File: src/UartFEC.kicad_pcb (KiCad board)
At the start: 2 copper layers, 24 x 27.9 mm, 16 parts, among them J1 B3B-XH-A, P1 105444-0001, U1 FT232RL

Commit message: Minor resistor move
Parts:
- moved R1 0.10 mm to (23.6, 44.1)
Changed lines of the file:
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@@
         (effects (font (size 0.8 0.6) (thickness 0.15)))
     )
-    (fp_text value "1K" (at 0 1.7) (layer "F.SilkS")
+    (fp_text value "1K" (at 0 1.5) (layer "F.SilkS")
         (effects (font (size 0.8 0.6) (thickness 0.15)))
     )
@@
   )
   (footprint "Medo64:R (0805)" (layer "F.Cu")
-    (at 23.7 44.1 180)
+    (at 23.6 44.1 180)
     (tags "RESC2013X70N")
     (attr smd)
@@
         (effects (font (size 0.8 0.6) (thickness 0.15)))
     )
-    (fp_text value "1K" (at 0 1.7) (layer "F.SilkS")
+    (fp_text value "1K" (at 0 1.5) (layer "F.SilkS")
         (effects (font (size 0.8 0.6) (thickness 0.15)))
     )
@@
   (segment (start 34.475 33.625) (end 35.5 33.625) (width 0.35) (layer "F.Cu") (net 2))
   (segment (start 32.95 35.15) (end 34.475 33.625) (width 0.35) (layer "F.Cu") (net 2))
-  (segment (start 23.556148 39.656148) (end 23.556148 42.756148) (width 0.2) (layer "F.Cu") (net 3))
   (segment (start 43.211786 36.988214) (end 43.208226 36.9881) (width 0.2) (layer "F.Cu") (net 3))
   (segment (start 43.3 27.6) (end 43.6 27.9) (width 0.2) (layer "F.Cu") (net 3))
@@
   (segment (start 42.5 26.6) (end 42.5 27.6) (width 0.2) (layer "F.Cu") (net 3))
   (segment (start 28.5 28.525) (end 26.8 28.525) (width 0.2) (layer "F.Cu") (net 3))
-  (segment (start 21.7 36.5) (end 23.510568 38.310568) (width 0.2) (layer "F.Cu") (net 3))
   (segment (start 40.400008 27.6) (end 42.5 27.6) (width 0.2) (layer "F.Cu") (net 3))
   (segment (start 43.6 36.6) (end 43.211786 36.988214) (width 0.2) (layer "F.Cu") (net 3))
+  (segment (start 23.556148 43.106148) (end 24.55 44.1) (width 0.2) (layer "F.Cu") (net 3))
+  (segment (start 23.556148 39.656148) (end 23.556148 43.106148) (width 0.2) (layer "F.Cu") (net 3))
   (segment (start 26.725 28.6) (end 26.8 28.525) (width 0.2) (layer "F.Cu") (net 3))
   (segment (start 43.208226 36.9881) (end 43.08487 37) (width 0.2) (layer "F.Cu") (net 3))
   (segment (start 40.4 27.599992) (end 40.400008 27.6) (width 0.2) (layer "F.Cu") (net 3))
   (segment (start 40.4 26.55) (end 40.4 27.599992) (width 0.2) (layer "F.Cu") (net 3))
+  (segment (start 21.7 36.5) (end 23.510568 38.310568) (width 0.2) (layer "F.Cu") (net 3))
   (segment (start 21.7 36.5) (end 21.3 36.1) (width 0.2) (layer "F.Cu") (net 3))
   (segment (start 40.436628 43.086628) (end 41.4 44.05) (width 0.2) (layer "F.Cu") (net 3))
-  (segment (start 23.556148 42.756148) (end 24.65 43.85) (width 0.2) (layer "F.Cu") (net 3))
+  (segment (start 23.510568 38.310568) (end 23.510568 39.302643) (width 0.2) (layer "F.Cu") (net 3))
   (segment (start 42.5 27.6) (end 43.3 27.6) (width 0.2) (layer "F.Cu") (net 3))
   (segment (start 25.7 28.6) (end 26.725 28.6) (width 0.2) (layer "F.Cu") (net 3))
-  (segment (start 23.510568 38.310568) (end 23.510568 39.302643) (width 0.2) (layer "F.Cu") (net 3))
   (segment (start 42.101103 37) (end 40.436628 38.664475) (width 0.2) (layer "F.Cu") (net 3))
   (segment (start 23.510568 39.302643) (end 23.556148 39.656148) (width 0.2) (layer "F.Cu") (net 3))

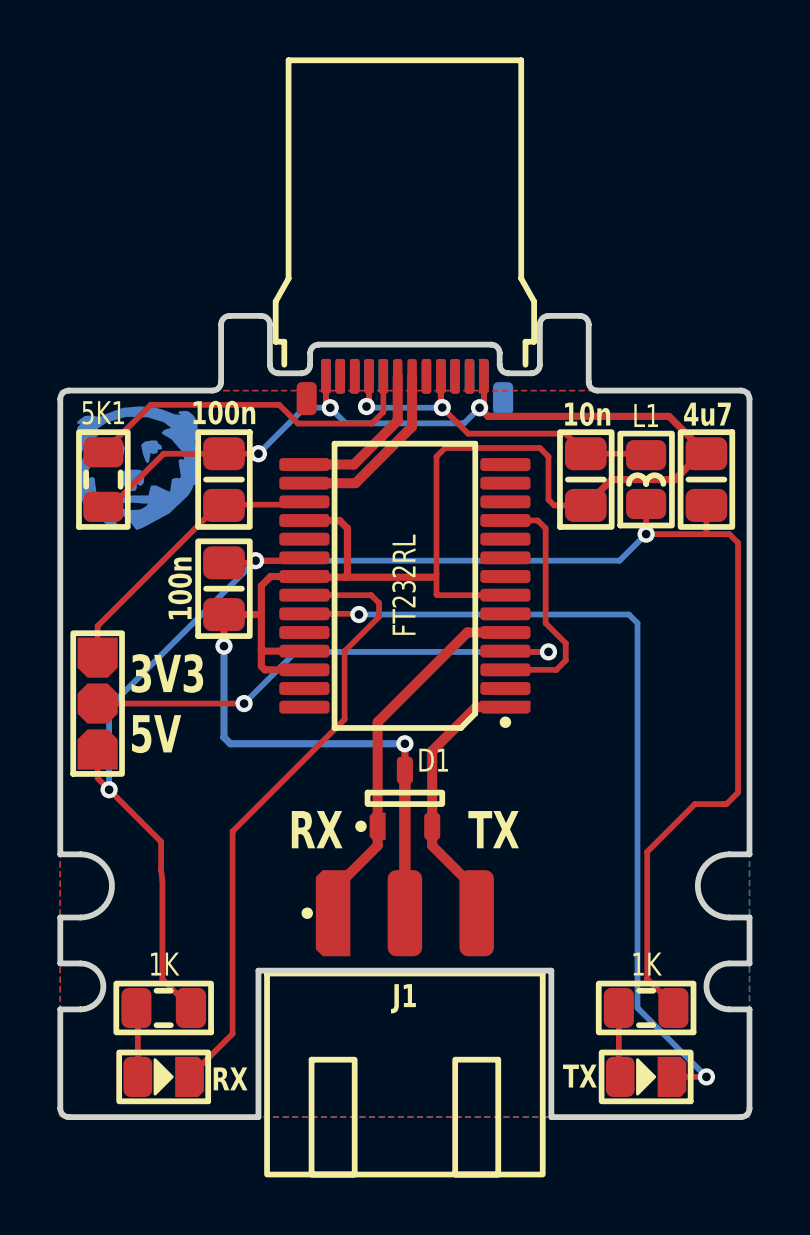
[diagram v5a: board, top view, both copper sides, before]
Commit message: Moved LEDs to bottom
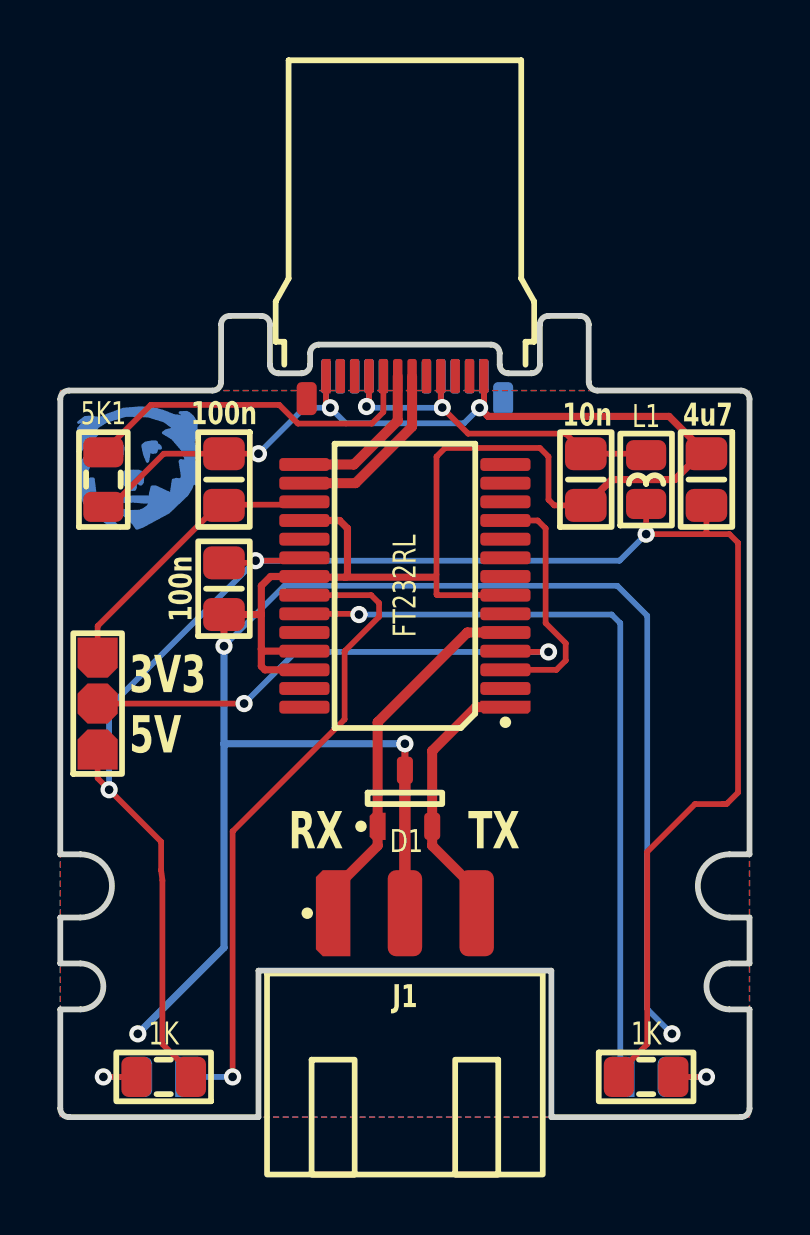
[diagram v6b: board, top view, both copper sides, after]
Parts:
- DS1, DS2: moved to B.Cu
- moved R1 2.40 mm to (23.6, 46.5)
- moved R2 2.40 mm to (40.4, 46.5), turned to 0 degrees
- turned DS2 to 0 degrees
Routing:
- net GND: track 81.2 -> 123.7 mm, vias 5 -> 7
- net 5V: track 61.1 -> 65.7 mm
- net LED_TXD: track 29.7 -> 26.7 mm, vias 2 -> 1
- net LED_RXD: track 21.9 -> 22.8 mm, vias 0 -> 1
- net LED_RXD': vias 0 -> 1
- net LED_TXD': vias 0 -> 1

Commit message: Refactored LED control for standby
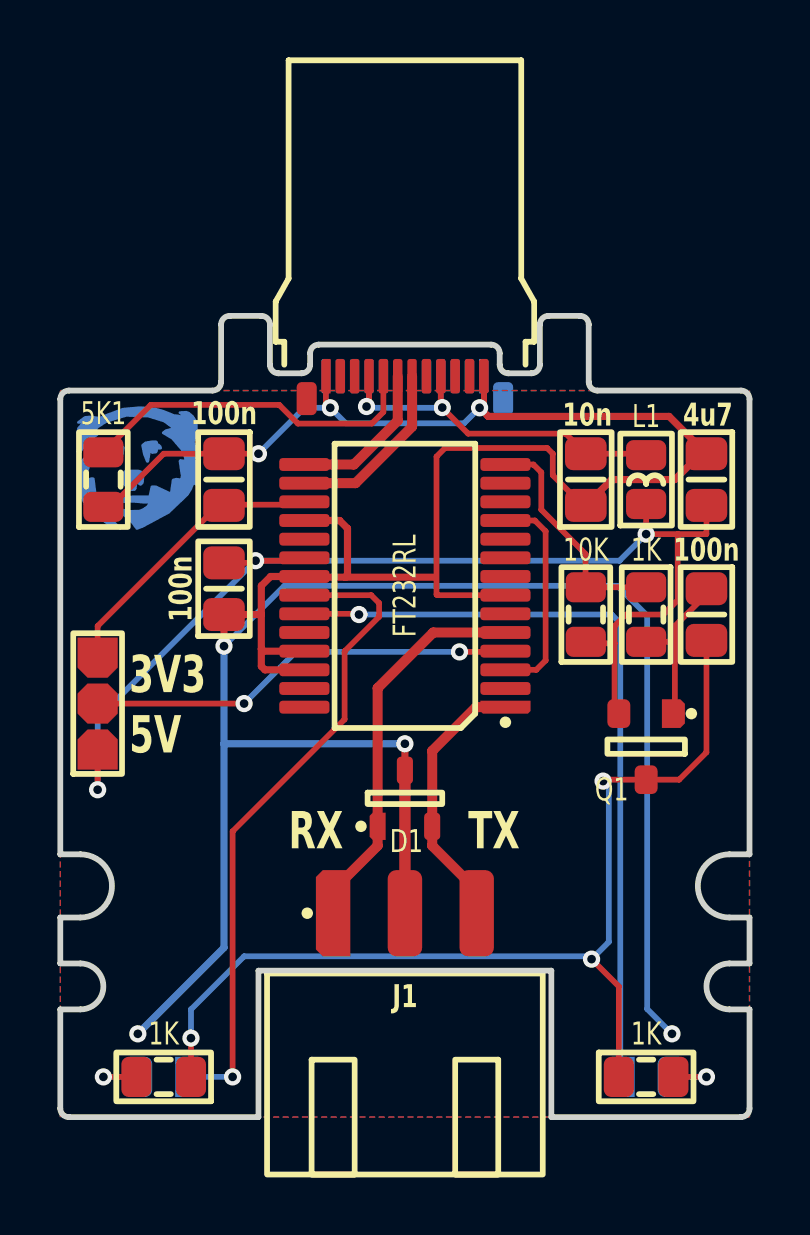
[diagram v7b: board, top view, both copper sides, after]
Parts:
- added C5: 100n, Medo64:C (0805), F.Cu at (42.5, 30.4)
- added Q1: DMP3099L-13, Medo64:Q MOSFET-P (SOT23-3), F.Cu at (40.4, 35.0)
- added R3: 1K, Medo64:R (0805), F.Cu at (40.4, 30.4)
- added R5: 10K, Medo64:R (0805), F.Cu at (38.3, 30.4)
- renumbered R3 to R4
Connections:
- R1 pad 1: 5V -> 5V_SW
- R2 pad 1: 5V -> 5V_SW
- U1 pad 14: (no net) -> PWREN#
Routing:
- net 5V_SW: track 0.00 -> 36.0 mm, vias 0 -> 3
- net 5V: track 65.7 -> 41.3 mm
- net PWREN#: track 0.00 -> 8.11 mm
- net PWREN#': track 0.00 -> 5.56 mm
- net Vio: track 17.5 -> 14.6 mm
- net RTS_CTS: track 8.64 -> 7.59 mm
- net RXD: track 12.2 -> 12.9 mm
- net GND: track 123.7 -> 123.1 mm

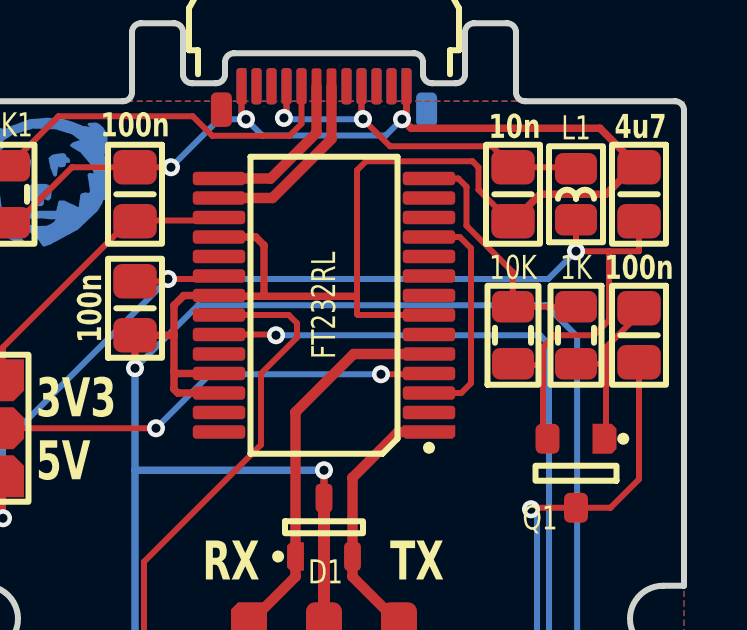
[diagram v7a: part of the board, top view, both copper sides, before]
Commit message: Removed internal RTS/CTS connection
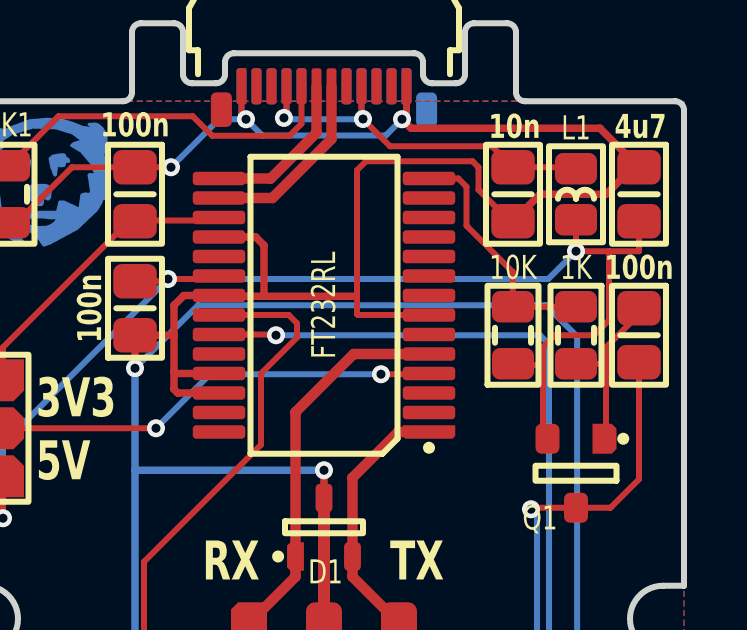
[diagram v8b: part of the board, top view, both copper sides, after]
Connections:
- U1 pad 11: RTS_CTS -> (no net)
- U1 pad 3: RTS_CTS -> (no net)
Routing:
- net RTS_CTS: track 7.59 -> 0.00 mm
